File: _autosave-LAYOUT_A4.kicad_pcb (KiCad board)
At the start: 2 copper layers, 212.1 x 207 mm, 122 parts, among them K1 CONN_3, SW1 DPST, SW10 DPST, SW11 DPST, SW12 DPST, SW13 DPST, SW14 DPST, SW15 DPST, SW16 DPST, SW2 DPST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

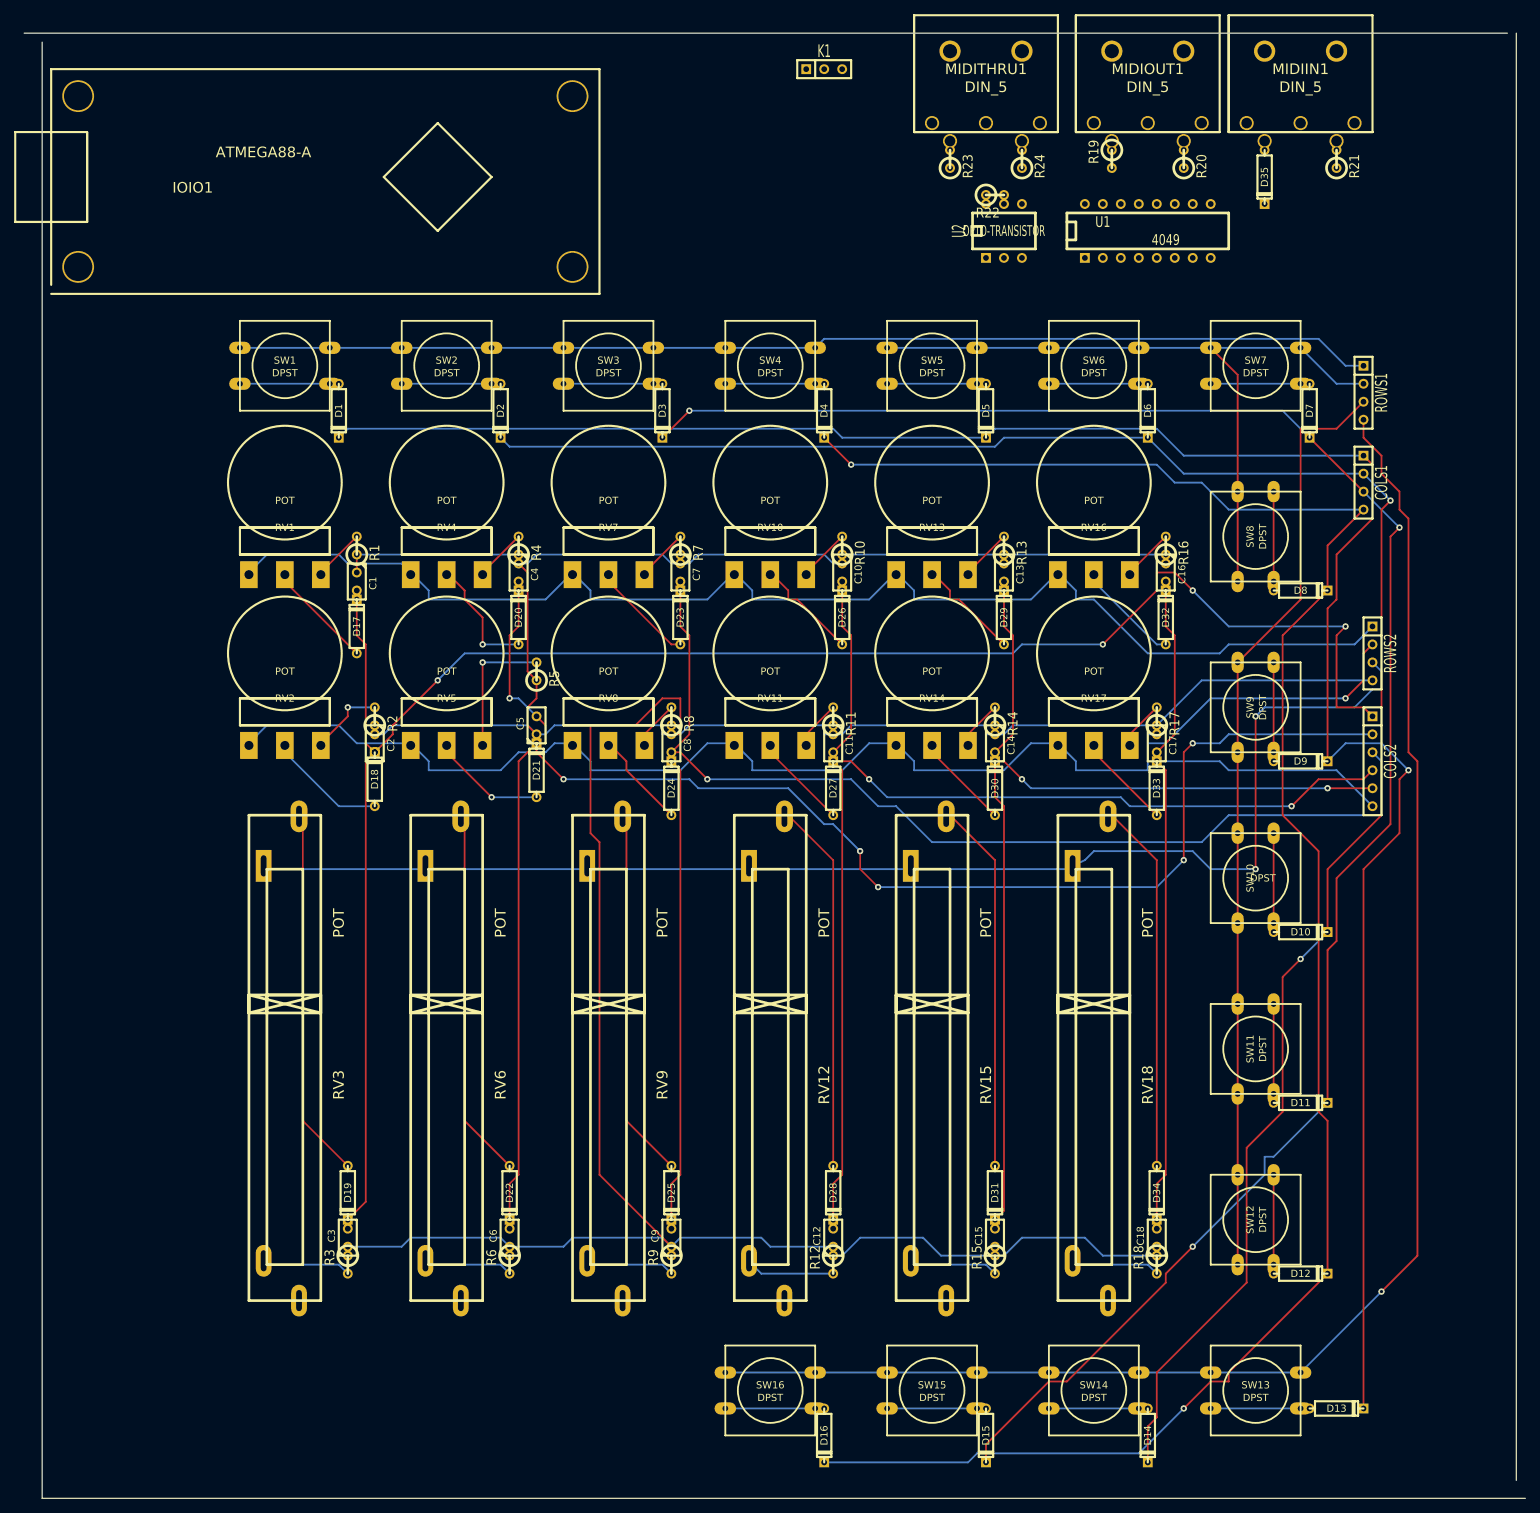
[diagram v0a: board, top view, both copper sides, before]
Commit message: Layout complete with parts
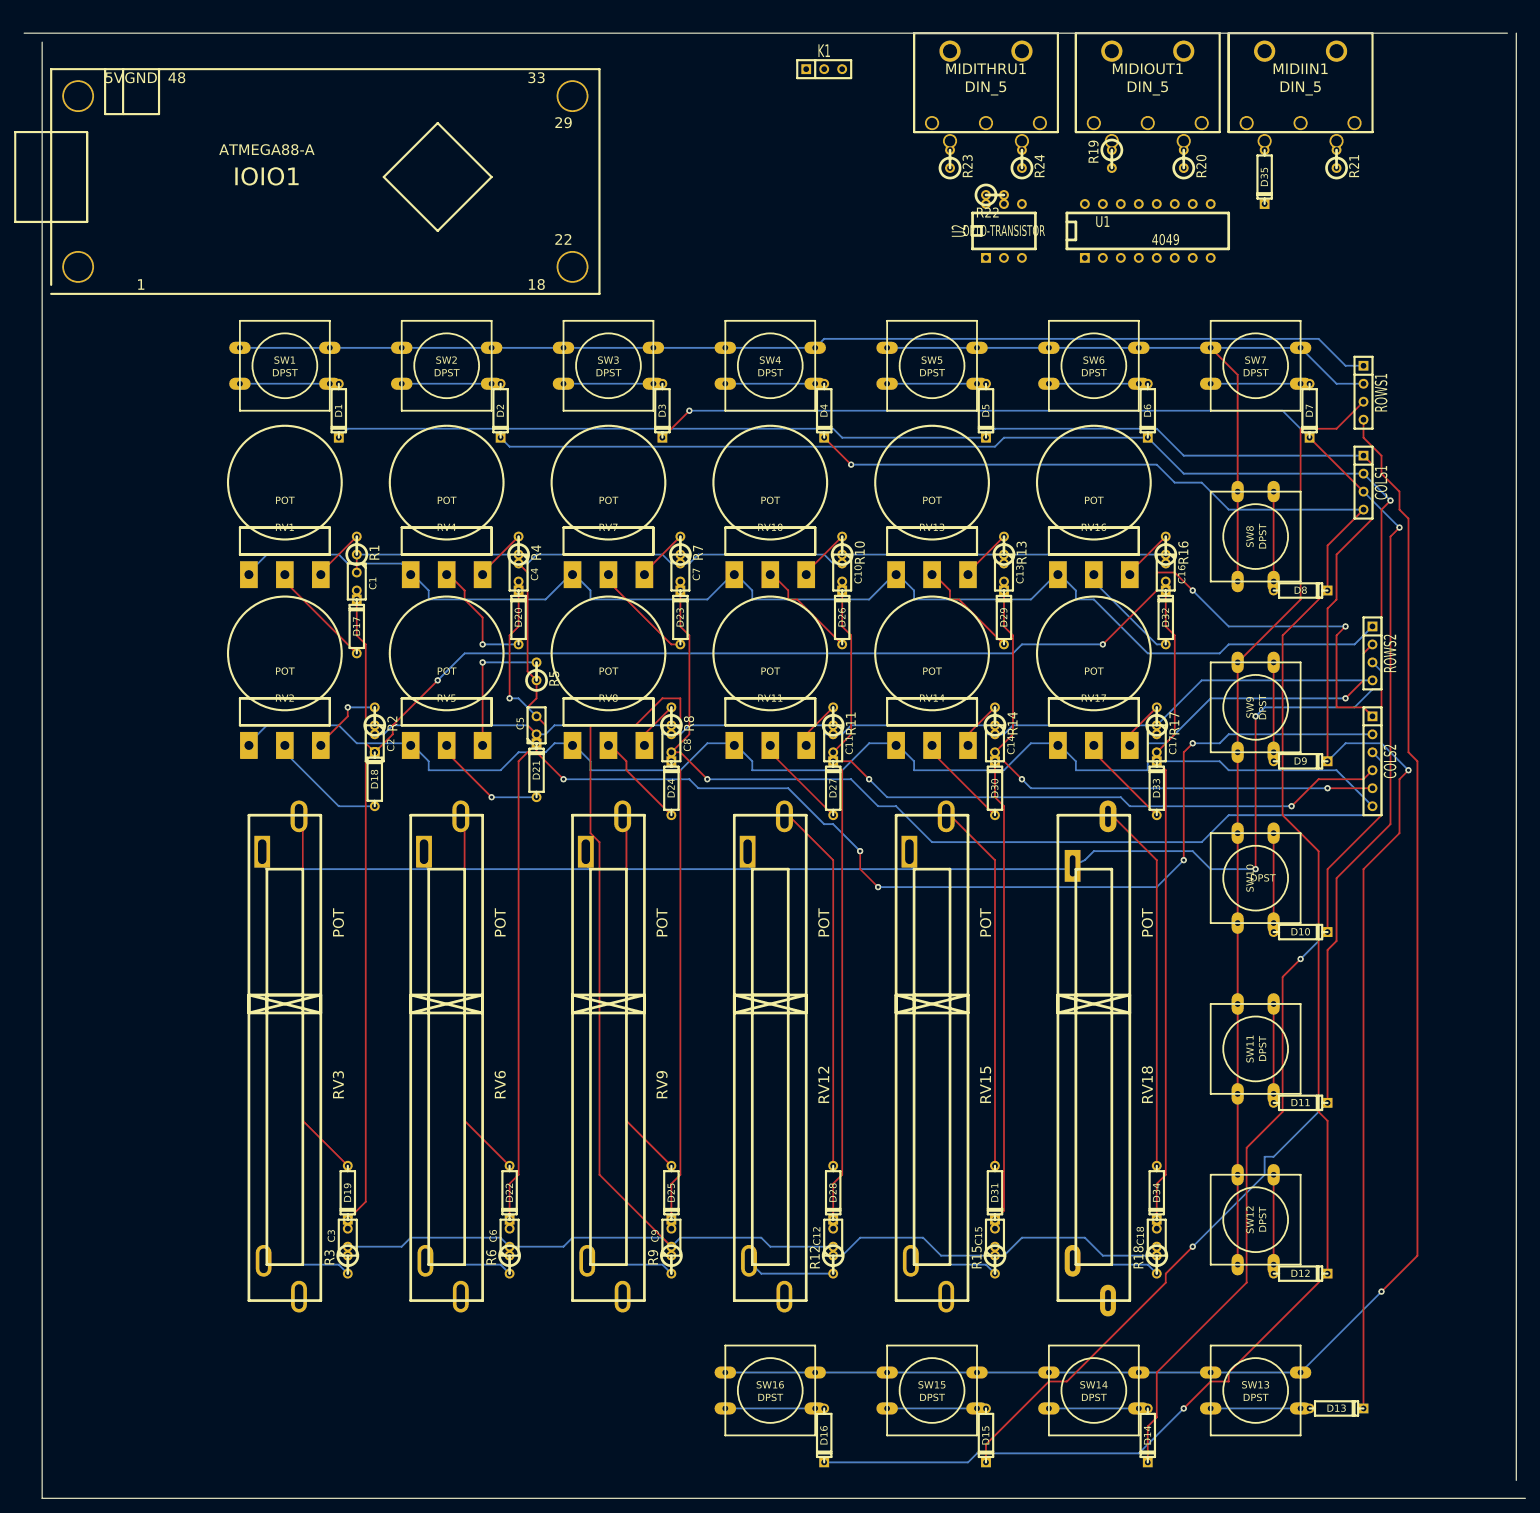
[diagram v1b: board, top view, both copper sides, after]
